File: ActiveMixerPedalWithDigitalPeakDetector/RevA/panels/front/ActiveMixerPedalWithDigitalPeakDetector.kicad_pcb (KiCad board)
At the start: 2 copper layers, 112.5 x 86.4 mm, 5 parts

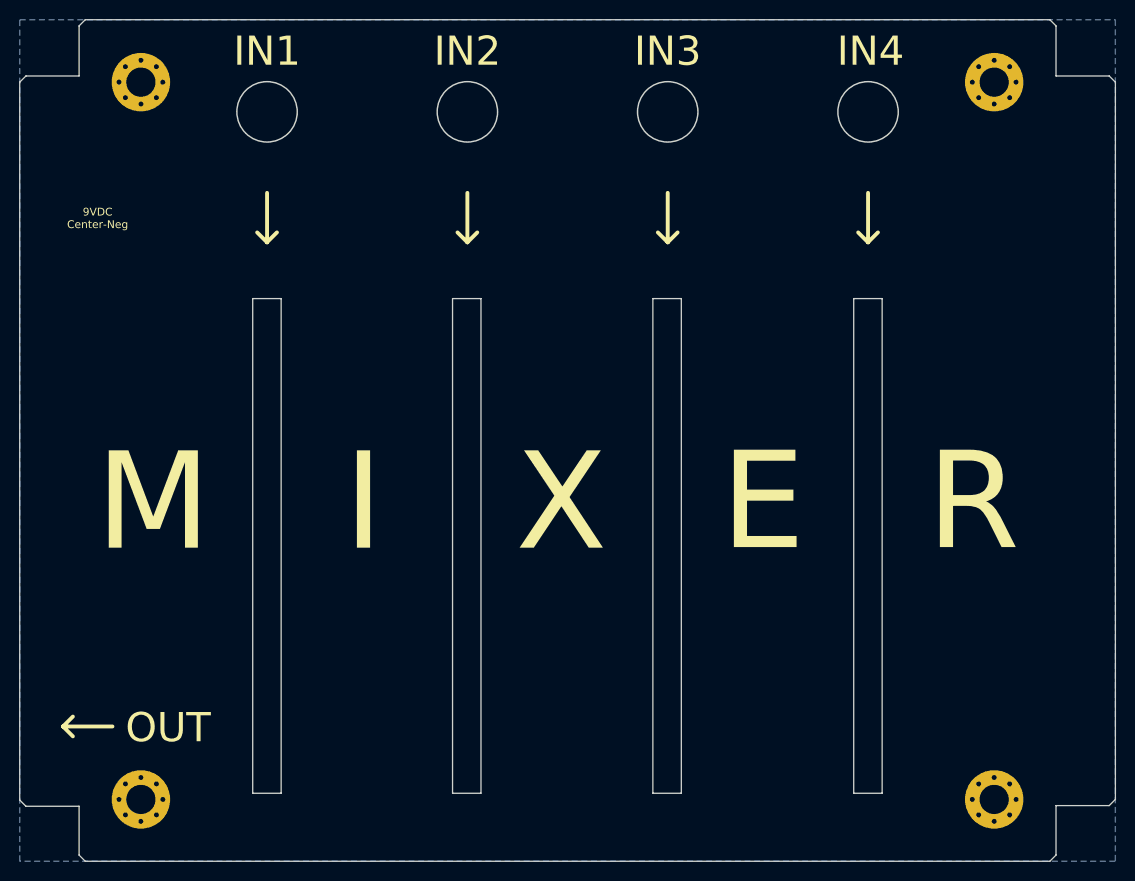
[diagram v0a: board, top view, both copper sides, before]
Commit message: updated front/back panel layout and gerbers
- Changed mount holes to non-via
- Changed BCu plane to FCu plane (same side as FCu silkscreen)
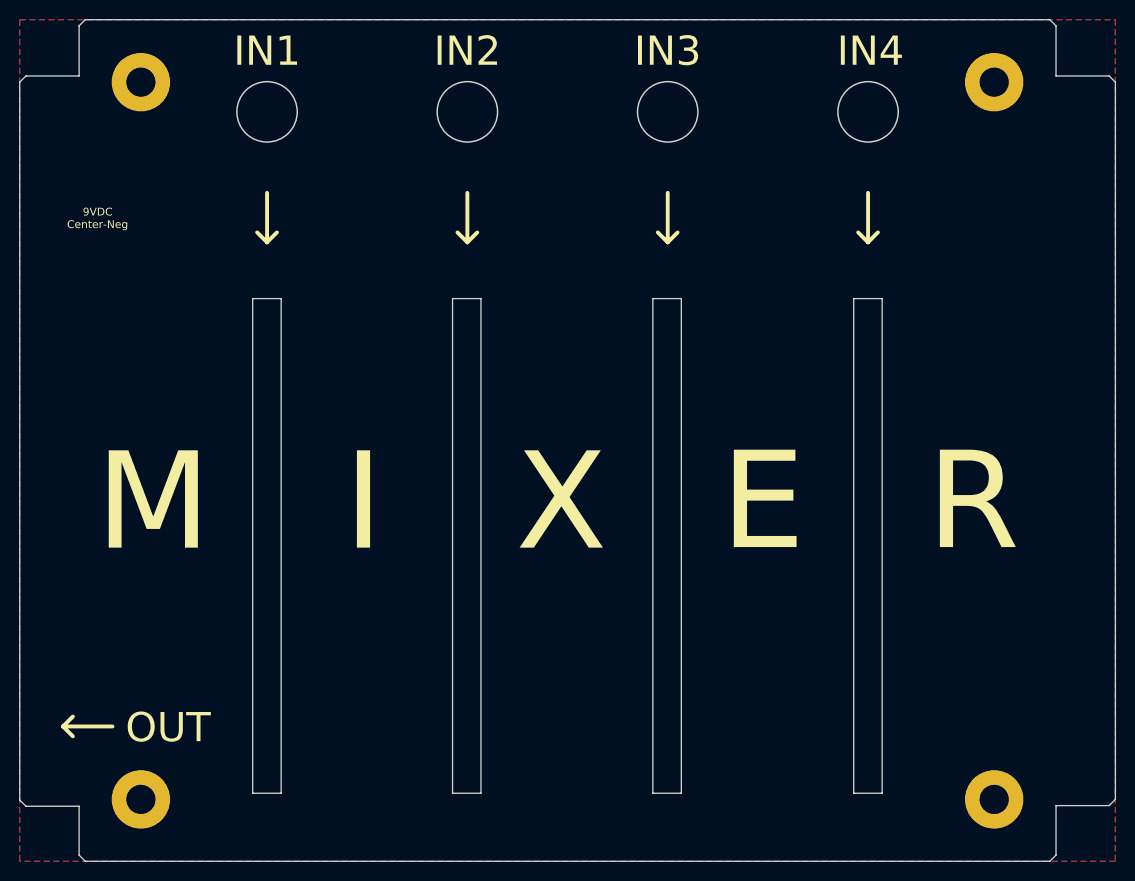
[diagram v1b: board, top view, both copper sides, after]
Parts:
- removed the REF** at (54.6, 134.6)
- removed the REF** at (142.2, 134.6)
- removed the REF** at (142.2, 61.0)
- added REF**: MountingHole_3mm_Pad, MountingHole:MountingHole_3mm_Pad, F.Cu at (54.6, 134.6)
- added REF**: MountingHole_3mm_Pad, MountingHole:MountingHole_3mm_Pad, F.Cu at (142.2, 134.6)
- added REF**: MountingHole_3mm_Pad, MountingHole:MountingHole_3mm_Pad, F.Cu at (142.2, 61.0)
- REF**: value MountingHole_3mm_Pad_Via -> MountingHole_3mm_Pad; footprint MountingHole:MountingHole_3mm_Pad_Via -> MountingHole:MountingHole_3mm_Pad
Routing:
- added copper zone on F.Cu, net (none)
- removed copper zone on B.Cu, net (none)
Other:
- board text removed: "-3V"
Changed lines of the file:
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@@
   (general
     (thickness 1.6)
-    (drawings 70)
+    (drawings 66)
     (tracks 0)
     (zones 0)
@@
     (diff_pair_gap 0.127)
   )
-  (module MountingHole:MountingHole_3mm_Pad_Via locked (layer F.Cu)
+  (module MountingHole:MountingHole_3mm_Pad locked (layer F.Cu)
     (at 54.61 134.62)
     (descr "Mounting Hole 3mm")
@@
       (effects (font (size 1 1) (thickness 0.15)))
     )
-    (fp_text value MountingHole_3mm_Pad_Via (at 0 4) (layer F.Fab)
+    (fp_text value MountingHole_3mm_Pad (at 0 4) (layer F.Fab)
       (effects (font (size 1 1) (thickness 0.15)))
     )
@@
     )
     (pad 1 thru_hole circle (at 0 0) (size 6 6) (drill 3) (layers *.Cu *.Mask))
-    (pad 1 thru_hole circle (at 2.25 0) (size 0.8 0.8) (drill 0.5) (layers *.Cu *.Mask))
-    (pad 1 thru_hole circle (at 1.59099 1.59099) (size 0.8 0.8) (drill 0.5) (layers *.Cu *.Mask))
-    (pad 1 thru_hole circle (at 0 2.25) (size 0.8 0.8) (drill 0.5) (layers *.Cu *.Mask))
-    (pad 1 thru_hole circle (at -1.59099 1.59099) (size 0.8 0.8) (drill 0.5) (layers *.Cu *.Mask))
-    (pad 1 thru_hole circle (at -2.25 0) (size 0.8 0.8) (drill 0.5) (layers *.Cu *.Mask))
-    (pad 1 thru_hole circle (at -1.59099 -1.59099) (size 0.8 0.8) (drill 0.5) (layers *.Cu *.Mask))
-    (pad 1 thru_hole circle (at 0 -2.25) (size 0.8 0.8) (drill 0.5) (layers *.Cu *.Mask))
-    (pad 1 thru_hole circle (at 1.59099 -1.59099) (size 0.8 0.8) (drill 0.5) (layers *.Cu *.Mask))
-  )
-  (module MountingHole:MountingHole_3mm_Pad_Via (layer F.Cu)
+  )
+  (module MountingHole:MountingHole_3mm_Pad (layer F.Cu)
     (at 142.24 134.62)
     (descr "Mounting Hole 3mm")
@@
       (effects (font (size 1 1) (thickness 0.15)))
     )
-    (fp_text value MountingHole_3mm_Pad_Via (at 0 4) (layer F.Fab)
+    (fp_text value MountingHole_3mm_Pad (at 0 4) (layer F.Fab)
       (effects (font (size 1 1) (thickness 0.15)))
     )
@@
     )
     (pad 1 thru_hole circle (at 0 0) (size 6 6) (drill 3) (layers *.Cu *.Mask))
-    (pad 1 thru_hole circle (at 2.25 0) (size 0.8 0.8) (drill 0.5) (layers *.Cu *.Mask))
-    (pad 1 thru_hole circle (at 1.59099 1.59099) (size 0.8 0.8) (drill 0.5) (layers *.Cu *.Mask))
-    (pad 1 thru_hole circle (at 0 2.25) (size 0.8 0.8) (drill 0.5) (layers *.Cu *.Mask))
-    (pad 1 thru_hole circle (at -1.59099 1.59099) (size 0.8 0.8) (drill 0.5) (layers *.Cu *.Mask))
-    (pad 1 thru_hole circle (at -2.25 0) (size 0.8 0.8) (drill 0.5) (layers *.Cu *.Mask))
-    (pad 1 thru_hole circle (at -1.59099 -1.59099) (size 0.8 0.8) (drill 0.5) (layers *.Cu *.Mask))
-    (pad 1 thru_hole circle (at 0 -2.25) (size 0.8 0.8) (drill 0.5) (layers *.Cu *.Mask))
-    (pad 1 thru_hole circle (at 1.59099 -1.59099) (size 0.8 0.8) (drill 0.5) (layers *.Cu *.Mask))
-  )
-  (module MountingHole:MountingHole_3mm_Pad_Via locked (layer F.Cu)
+  )
+  (module MountingHole:MountingHole_3mm_Pad locked (layer F.Cu)
     (at 142.24 60.96)
     (descr "Mounting Hole 3mm")
@@
       (effects (font (size 1 1) (thickness 0.15)))
     )
-    (fp_text value MountingHole_3mm_Pad_Via (at 0 4) (layer F.Fab)
+    (fp_text value MountingHole_3mm_Pad (at 0 4) (layer F.Fab)
       (effects (font (size 1 1) (thickness 0.15)))
     )
@@
     )
     (pad 1 thru_hole circle (at 0 0) (size 6 6) (drill 3) (layers *.Cu *.Mask))
-    (pad 1 thru_hole circle (at 2.25 0) (size 0.8 0.8) (drill 0.5) (layers *.Cu *.Mask))
-    (pad 1 thru_hole circle (at 1.59099 1.59099) (size 0.8 0.8) (drill 0.5) (layers *.Cu *.Mask))
-    (pad 1 thru_hole circle (at 0 2.25) (size 0.8 0.8) (drill 0.5) (layers *.Cu *.Mask))
-    (pad 1 thru_hole circle (at -1.59099 1.59099) (size 0.8 0.8) (drill 0.5) (layers *.Cu *.Mask))
-    (pad 1 thru_hole circle (at -2.25 0) (size 0.8 0.8) (drill 0.5) (layers *.Cu *.Mask))
-    (pad 1 thru_hole circle (at -1.59099 -1.59099) (size 0.8 0.8) (drill 0.5) (layers *.Cu *.Mask))
-    (pad 1 thru_hole circle (at 0 -2.25) (size 0.8 0.8) (drill 0.5) (layers *.Cu *.Mask))
-    (pad 1 thru_hole circle (at 1.59099 -1.59099) (size 0.8 0.8) (drill 0.5) (layers *.Cu *.Mask))
-  )
-  (module MountingHole:MountingHole_3mm_Pad_Via locked (layer F.Cu)
+  )
+  (module MountingHole:MountingHole_3mm_Pad locked (layer F.Cu)
     (at 54.61 60.96)
     (descr "Mounting Hole 3mm")
@@
       (effects (font (size 1 1) (thickness 0.15)))
     )
-    (fp_text value MountingHole_3mm_Pad_Via (at 0 4) (layer F.Fab)
+    (fp_text value MountingHole_3mm_Pad (at 0 4) (layer F.Fab)
       (effects (font (size 1 1) (thickness 0.15)))
     )
@@
       (effects (font (size 1 1) (thickness 0.15)))
     )
-    (pad 1 thru_hole circle (at 1.59099 -1.59099) (size 0.8 0.8) (drill 0.5) (layers *.Cu *.Mask))
-    (pad 1 thru_hole circle (at 0 -2.25) (size 0.8 0.8) (drill 0.5) (layers *.Cu *.Mask))
-    (pad 1 thru_hole circle (at -1.59099 -1.59099) (size 0.8 0.8) (drill 0.5) (layers *.Cu *.Mask))
-    (pad 1 thru_hole circle (at -2.25 0) (size 0.8 0.8) (drill 0.5) (layers *.Cu *.Mask))
-    (pad 1 thru_hole circle (at -1.59099 1.59099) (size 0.8 0.8) (drill 0.5) (layers *.Cu *.Mask))
-    (pad 1 thru_hole circle (at 0 2.25) (size 0.8 0.8) (drill 0.5) (layers *.Cu *.Mask))
-    (pad 1 thru_hole circle (at 1.59099 1.59099) (size 0.8 0.8) (drill 0.5) (layers *.Cu *.Mask))
-    (pad 1 thru_hole circle (at 2.25 0) (size 0.8 0.8) (drill 0.5) (layers *.Cu *.Mask))
     (pad 1 thru_hole circle (at 0 0) (size 6 6) (drill 3) (layers *.Cu *.Mask))
   )
@@
   (gr_line (start 110.109 83.185) (end 110.109 133.985) (layer Edge.Cuts) (width 0.05))
   (gr_line (start 107.188 83.185) (end 110.109 83.185) (layer Edge.Cuts) (width 0.05))
-  (gr_line (start -74.8665 46.9265) (end -76.6445 46.9265) (layer Dwgs.User) (width 0.15))
-  (gr_line (start -74.8665 40.64) (end -76.6445 40.64) (layer Dwgs.User) (width 0.15))
-  (gr_line (start -75.7555 40.64) (end -75.7555 46.9265) (layer Dwgs.User) (width 0.15))
   (gr_circle (center 129.286 64.008) (end 132.386465 64.008) (layer Edge.Cuts) (width 0.15))
   (gr_circle (center 108.712 64.008) (end 111.812465 64.008) (layer Edge.Cuts) (width 0.15))
   (gr_circle (center 88.138 64.008) (end 91.238465 64.008) (layer Edge.Cuts) (width 0.15))
   (gr_circle (center 67.564 64.008) (end 70.664465 64.008) (layer Edge.Cuts) (width 0.15))
-  (gr_text -3V (at 54.102 137.6045) (layer B.SilkS)
-    (effects (font (size 0.8 0.8) (thickness 0.15)) (justify mirror))
-  )
   (gr_line (start 67.564 77.4065) (end 67.564 72.3265) (layer F.SilkS) (width 0.4))
   (gr_line (start 67.564 77.4065) (end 66.548 76.3905) (layer F.SilkS) (width 0.4))
@@
   (gr_line (start 48.895 140.97) (end 48.26 140.335) (layer Edge.Cuts) (width 0.05))
   (gr_line (start 147.955 140.97) (end 48.895 140.97) (layer Edge.Cuts) (width 0.05))
-  (zone (net 0) (net_name "") (layer B.Cu) (hatch edge 0.508)
+  (zone (net 0) (net_name "") (layer F.Cu) (hatch edge 0.508)
     (priority 1)
     (connect_pads yes (clearance 0.508))

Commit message: updated frontpanel layout
moved silk screen
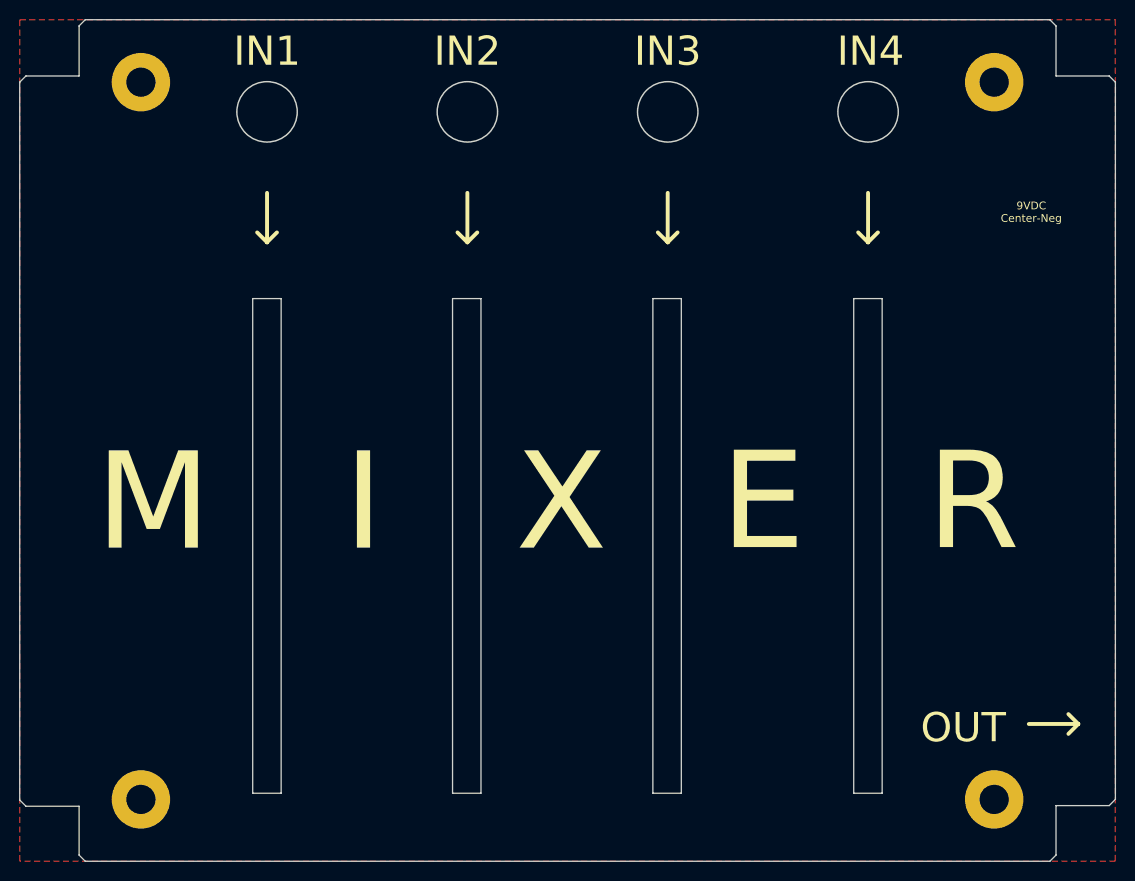
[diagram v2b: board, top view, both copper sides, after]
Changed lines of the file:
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@@
-(kicad_pcb (version 20171130) (host pcbnew "(5.1.6-0-10_14)")
+(kicad_pcb (version 20171130) (host pcbnew 5.1.6-c6e7f7d~87~ubuntu18.04.1)
   (general
     (thickness 1.6)
@@
       (effects (font (size 1 1) (thickness 0.15)))
     )
-    (fp_circle (center 0 0) (end 3.25 0) (layer F.CrtYd) (width 0.05))
-    (fp_circle (center 0 0) (end 3 0) (layer Cmts.User) (width 0.15))
+    (fp_circle (center 0 0) (end 3 0) (layer Cmts.User) (width 0.15))
+    (fp_circle (center 0 0) (end 3.25 0) (layer F.CrtYd) (width 0.05))
     (fp_text user %R (at 0.3 0) (layer F.Fab)
       (effects (font (size 1 1) (thickness 0.15)))
@@
       (effects (font (size 1 1) (thickness 0.15)))
     )
-    (fp_circle (center 0 0) (end 3.25 0) (layer F.CrtYd) (width 0.05))
-    (fp_circle (center 0 0) (end 3 0) (layer Cmts.User) (width 0.15))
+    (fp_circle (center 0 0) (end 3 0) (layer Cmts.User) (width 0.15))
+    (fp_circle (center 0 0) (end 3.25 0) (layer F.CrtYd) (width 0.05))
     (fp_text user %R (at 0.3 0) (layer F.Fab)
       (effects (font (size 1 1) (thickness 0.15)))
@@
       (effects (font (size 1 1) (thickness 0.15)))
     )
-    (fp_circle (center 0 0) (end 3.25 0) (layer F.CrtYd) (width 0.05))
-    (fp_circle (center 0 0) (end 3 0) (layer Cmts.User) (width 0.15))
+    (fp_circle (center 0 0) (end 3 0) (layer Cmts.User) (width 0.15))
+    (fp_circle (center 0 0) (end 3.25 0) (layer F.CrtYd) (width 0.05))
     (fp_text user %R (at 0.3 0) (layer F.Fab)
       (effects (font (size 1 1) (thickness 0.15)))
@@
       (effects (font (size 1 1) (thickness 0.15)))
     )
-    (fp_circle (center 0 0) (end 3.25 0) (layer F.CrtYd) (width 0.05))
-    (fp_circle (center 0 0) (end 3 0) (layer Cmts.User) (width 0.15))
+    (fp_circle (center 0 0) (end 3 0) (layer Cmts.User) (width 0.15))
+    (fp_circle (center 0 0) (end 3.25 0) (layer F.CrtYd) (width 0.05))
     (fp_text user %R (at 0.3 0) (layer F.Fab)
       (effects (font (size 1 1) (thickness 0.15)))
@@
       (effects (font (size 1 1) (thickness 0.15)))
     )
+    (fp_line (start 43.2435 -49.53) (end 42.6085 -50.165) (layer Dwgs.User) (width 0.12))
+    (fp_line (start 36.83 -56.261) (end 37.465 -55.626) (layer Dwgs.User) (width 0.12))
+    (fp_line (start -37.5285 -55.626) (end -36.8935 -56.261) (layer Dwgs.User) (width 0.12))
+    (fp_line (start -42.545 -50.165) (end -43.18 -49.53) (layer Dwgs.User) (width 0.12))
+    (fp_line (start -36.83 56.261) (end -37.465 55.626) (layer Dwgs.User) (width 0.12))
+    (fp_line (start -42.545 50.165) (end -43.18 49.53) (layer Dwgs.User) (width 0.12))
+    (fp_line (start 42.6085 50.165) (end 43.2435 49.53) (layer Dwgs.User) (width 0.12))
+    (fp_line (start 36.83 56.261) (end 37.465 55.626) (layer Dwgs.User) (width 0.12))
+    (fp_line (start -37.5285 -50.165) (end -42.545 -50.165) (layer Dwgs.User) (width 0.12))
+    (fp_line (start -37.5285 -55.626) (end -37.5285 -50.165) (layer Dwgs.User) (width 0.12))
+    (fp_line (start 37.465 -50.165) (end 37.465 -55.626) (layer Dwgs.User) (width 0.12))
+    (fp_line (start 42.6085 -50.165) (end 37.465 -50.165) (layer Dwgs.User) (width 0.12))
+    (fp_line (start 37.465 50.165) (end 42.6085 50.165) (layer Dwgs.User) (width 0.12))
+    (fp_line (start 37.465 55.626) (end 37.465 50.165) (layer Dwgs.User) (width 0.12))
+    (fp_line (start -37.465 50.165) (end -42.545 50.165) (layer Dwgs.User) (width 0.12))
+    (fp_line (start -37.465 55.626) (end -37.465 50.165) (layer Dwgs.User) (width 0.12))
+    (fp_line (start 43.2435 49.53) (end 43.2435 -49.53) (layer Dwgs.User) (width 0.12))
+    (fp_line (start -36.8935 -56.261) (end 36.83 -56.261) (layer Dwgs.User) (width 0.12))
+    (fp_line (start -36.83 56.261) (end 36.83 56.261) (layer Dwgs.User) (width 0.12))
+    (fp_line (start -43.18 49.53) (end -43.18 -49.53) (layer Dwgs.User) (width 0.12))
+    (fp_line (start -44.704 56.896) (end -44.704 -56.896) (layer Cmts.User) (width 0.12))
+    (fp_line (start 44.7675 56.896) (end -44.704 56.896) (layer Cmts.User) (width 0.12))
+    (fp_line (start 44.7675 -56.896) (end 44.7675 56.896) (layer Cmts.User) (width 0.12))
+    (fp_line (start -44.704 -56.896) (end 44.7675 -56.896) (layer Cmts.User) (width 0.12))
+    (fp_line (start -46.99 -59.7535) (end -46.99 59.7535) (layer Cmts.User) (width 0.12))
+    (fp_line (start 47.0535 59.7535) (end -46.99 59.7535) (layer Cmts.User) (width 0.12))
+    (fp_line (start -46.99 -59.7535) (end 47.0535 -59.7535) (layer Cmts.User) (width 0.12))
     (fp_line (start 47.0535 59.7535) (end 47.0535 -59.7535) (layer Cmts.User) (width 0.12))
-    (fp_line (start -46.99 -59.7535) (end 47.0535 -59.7535) (layer Cmts.User) (width 0.12))
-    (fp_line (start 47.0535 59.7535) (end -46.99 59.7535) (layer Cmts.User) (width 0.12))
-    (fp_line (start -46.99 -59.7535) (end -46.99 59.7535) (layer Cmts.User) (width 0.12))
-    (fp_line (start -44.704 -56.896) (end 44.7675 -56.896) (layer Cmts.User) (width 0.12))
-    (fp_line (start 44.7675 -56.896) (end 44.7675 56.896) (layer Cmts.User) (width 0.12))
-    (fp_line (start 44.7675 56.896) (end -44.704 56.896) (layer Cmts.User) (width 0.12))
-    (fp_line (start -44.704 56.896) (end -44.704 -56.896) (layer Cmts.User) (width 0.12))
-    (fp_line (start -43.18 49.53) (end -43.18 -49.53) (layer Dwgs.User) (width 0.12))
-    (fp_line (start -36.83 56.261) (end 36.83 56.261) (layer Dwgs.User) (width 0.12))
-    (fp_line (start -36.8935 -56.261) (end 36.83 -56.261) (layer Dwgs.User) (width 0.12))
-    (fp_line (start 43.2435 49.53) (end 43.2435 -49.53) (layer Dwgs.User) (width 0.12))
-    (fp_line (start -37.465 55.626) (end -37.465 50.165) (layer Dwgs.User) (width 0.12))
-    (fp_line (start -37.465 50.165) (end -42.545 50.165) (layer Dwgs.User) (width 0.12))
-    (fp_line (start 37.465 55.626) (end 37.465 50.165) (layer Dwgs.User) (width 0.12))
-    (fp_line (start 37.465 50.165) (end 42.6085 50.165) (layer Dwgs.User) (width 0.12))
-    (fp_line (start 42.6085 -50.165) (end 37.465 -50.165) (layer Dwgs.User) (width 0.12))
-    (fp_line (start 37.465 -50.165) (end 37.465 -55.626) (layer Dwgs.User) (width 0.12))
-    (fp_line (start -37.5285 -55.626) (end -37.5285 -50.165) (layer Dwgs.User) (width 0.12))
-    (fp_line (start -37.5285 -50.165) (end -42.545 -50.165) (layer Dwgs.User) (width 0.12))
-    (fp_line (start 36.83 56.261) (end 37.465 55.626) (layer Dwgs.User) (width 0.12))
-    (fp_line (start 42.6085 50.165) (end 43.2435 49.53) (layer Dwgs.User) (width 0.12))
-    (fp_line (start -42.545 50.165) (end -43.18 49.53) (layer Dwgs.User) (width 0.12))
-    (fp_line (start -36.83 56.261) (end -37.465 55.626) (layer Dwgs.User) (width 0.12))
-    (fp_line (start -42.545 -50.165) (end -43.18 -49.53) (layer Dwgs.User) (width 0.12))
-    (fp_line (start -37.5285 -55.626) (end -36.8935 -56.261) (layer Dwgs.User) (width 0.12))
-    (fp_line (start 36.83 -56.261) (end 37.465 -55.626) (layer Dwgs.User) (width 0.12))
-    (fp_line (start 43.2435 -49.53) (end 42.6085 -50.165) (layer Dwgs.User) (width 0.12))
   )
   (gr_line (start 129.286 77.4065) (end 130.302 76.3905) (layer F.SilkS) (width 0.4))
@@
   (gr_line (start 88.138 77.4065) (end 87.122 76.3905) (layer F.SilkS) (width 0.4))
   (gr_line (start 88.138 77.4065) (end 88.138 72.3265) (layer F.SilkS) (width 0.4))
-  (gr_text "9VDC\nCenter-Neg" (at 50.165 74.93) (layer F.SilkS)
+  (gr_text "9VDC\nCenter-Neg" (at 146.05 74.295) (layer F.SilkS)
     (effects (font (size 0.8 0.8) (thickness 0.15)))
   )
@@
     (effects (font (size 10 10) (thickness 1)))
   )
-  (gr_text OUT (at 57.404 127.254) (layer F.SilkS)
+  (gr_text OUT (at 139.065 127.254) (layer F.SilkS)
     (effects (font (size 3 3) (thickness 0.4)))
   )
@@
     (effects (font (size 3 3) (thickness 0.4)))
   )
-  (gr_line (start 46.609 127.127) (end 51.689 127.127) (layer F.SilkS) (width 0.4))
-  (gr_line (start 46.609 127.127) (end 47.625 126.111) (layer F.SilkS) (width 0.4))
-  (gr_line (start 46.609 127.127) (end 47.625 128.143) (layer F.SilkS) (width 0.4))
+  (gr_line (start 150.876 126.873) (end 145.796 126.873) (layer F.SilkS) (width 0.4))
+  (gr_line (start 150.876 126.873) (end 149.86 127.889) (layer F.SilkS) (width 0.4))
+  (gr_line (start 150.876 126.873) (end 149.86 125.857) (layer F.SilkS) (width 0.4))
   (gr_line (start 127.8128 83.185) (end 130.7338 83.185) (layer Edge.Cuts) (width 0.05))
   (gr_line (start 130.7338 133.985) (end 127.8128 133.985) (layer Edge.Cuts) (width 0.05))
